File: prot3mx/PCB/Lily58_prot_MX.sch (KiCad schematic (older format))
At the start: 115 parts, among them J1 LED, J2 4PIN, J3 OLED, P1 i2c_pin, P2 i2c_pin, SW1 SW_PUSH, SW10 SW_PUSH, SW11 SW_PUSH, SW12 SW_PUSH, SW13 SW_PUSH, SW14 SW_PUSH, SW15 SW_PUSH, SW16 SW_PUSH, SW17 SW_PUSH, SW18 SW_PUSH, SW19 SW_PUSH, SW2 SW_PUSH, SW20 SW_PUSH, SW21 SW_PUSH, SW22 SW_PUSH, SW23 SW_PUSH, SW24 SW_PUSH, SW25 SW_PUSH, SW26 SW_PUSH, SW27 SW_PUSH, SW28 SW_PUSH, SW29 SW_PUSH, SW3 SW_PUSH, SW30 ROT_ENC_SW, SW31 ROT_ENC_SW, SW32 ROT_ENC_SW, SW4 SW_PUSH, SW5 SW_PUSH, SW6 SW_PUSH, SW7 SW_PUSH, SW8 SW_PUSH, SW9 SW_PUSH, U1 ProMicro

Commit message: repositioned diodes, using original LED footprints
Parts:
- L1, L10, L11, L12, L13, L14, L15, L16, L17, L18, L19, L2, L20, L21, L22, L23, L24, L25, L26, L27, L28, L29, L3, L4, L5, L6, L7, L8, L9: footprint Lily58_prot_MX-footprint:SK6812MINI_rev_w_co -> Lily58_prot_MX-footprint:SK6812MINI_rev
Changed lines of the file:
@@
 F 0 "L1" H 2650 3900 50  0000 L CNN
 F 1 "SK6812MINI" H 2400 3300 50  0000 L CNN
-F 2 "Lily58_prot_MX-footprint:SK6812MINI_rev_w_co" H 2650 3350 50  0001 L TNN
+F 2 "Lily58_prot_MX-footprint:SK6812MINI_rev" H 2650 3350 50  0001 L TNN
 F 3 "" H 2700 3275 50  0001 L TNN
 	1    2600 3650
@@
 F 0 "L2" H 3250 3900 50  0000 L CNN
 F 1 "SK6812MINI" H 3000 3300 50  0000 L CNN
-F 2 "Lily58_prot_MX-footprint:SK6812MINI_rev_w_co" H 3250 3350 50  0001 L TNN
+F 2 "Lily58_prot_MX-footprint:SK6812MINI_rev" H 3250 3350 50  0001 L TNN
 F 3 "" H 3300 3275 50  0001 L TNN
 	1    3200 3650
@@
 F 0 "L3" H 3850 3900 50  0000 L CNN
 F 1 "SK6812MINI" H 3600 3300 50  0000 L CNN
-F 2 "Lily58_prot_MX-footprint:SK6812MINI_rev_w_co" H 3850 3350 50  0001 L TNN
+F 2 "Lily58_prot_MX-footprint:SK6812MINI_rev" H 3850 3350 50  0001 L TNN
 F 3 "" H 3900 3275 50  0001 L TNN
 	1    3800 3650
@@
 F 0 "L4" H 4450 3900 50  0000 L CNN
 F 1 "SK6812MINI" H 4200 3300 50  0000 L CNN
-F 2 "Lily58_prot_MX-footprint:SK6812MINI_rev_w_co" H 4450 3350 50  0001 L TNN
+F 2 "Lily58_prot_MX-footprint:SK6812MINI_rev" H 4450 3350 50  0001 L TNN
 F 3 "" H 4500 3275 50  0001 L TNN
 	1    4400 3650
@@
 F 0 "L5" H 5050 3900 50  0000 L CNN
 F 1 "SK6812MINI" H 4800 3300 50  0000 L CNN
-F 2 "Lily58_prot_MX-footprint:SK6812MINI_rev_w_co" H 5050 3350 50  0001 L TNN
+F 2 "Lily58_prot_MX-footprint:SK6812MINI_rev" H 5050 3350 50  0001 L TNN
 F 3 "" H 5100 3275 50  0001 L TNN
 	1    5000 3650
@@
 F 0 "L6" H 5650 3900 50  0000 L CNN
 F 1 "SK6812MINI" H 5400 3300 50  0000 L CNN
-F 2 "Lily58_prot_MX-footprint:SK6812MINI_rev_w_co" H 5650 3350 50  0001 L TNN
+F 2 "Lily58_prot_MX-footprint:SK6812MINI_rev" H 5650 3350 50  0001 L TNN
 F 3 "" H 5700 3275 50  0001 L TNN
 	1    5600 3650
@@
 F 0 "L7" H 2650 4750 50  0000 L CNN
 F 1 "SK6812MINI" H 2400 4150 50  0000 L CNN
-F 2 "Lily58_prot_MX-footprint:SK6812MINI_rev_w_co" H 2650 4200 50  0001 L TNN
+F 2 "Lily58_prot_MX-footprint:SK6812MINI_rev" H 2650 4200 50  0001 L TNN
 F 3 "" H 2700 4125 50  0001 L TNN
 	1    2600 4500
@@
 F 0 "L8" H 3250 4750 50  0000 L CNN
 F 1 "SK6812MINI" H 3000 4150 50  0000 L CNN
-F 2 "Lily58_prot_MX-footprint:SK6812MINI_rev_w_co" H 3250 4200 50  0001 L TNN
+F 2 "Lily58_prot_MX-footprint:SK6812MINI_rev" H 3250 4200 50  0001 L TNN
 F 3 "" H 3300 4125 50  0001 L TNN
 	1    3200 4500
@@
 F 0 "L9" H 3850 4750 50  0000 L CNN
 F 1 "SK6812MINI" H 3600 4150 50  0000 L CNN
-F 2 "Lily58_prot_MX-footprint:SK6812MINI_rev_w_co" H 3850 4200 50  0001 L TNN
+F 2 "Lily58_prot_MX-footprint:SK6812MINI_rev" H 3850 4200 50  0001 L TNN
 F 3 "" H 3900 4125 50  0001 L TNN
 	1    3800 4500
@@
 F 0 "L10" H 4450 4750 50  0000 L CNN
 F 1 "SK6812MINI" H 4200 4150 50  0000 L CNN
-F 2 "Lily58_prot_MX-footprint:SK6812MINI_rev_w_co" H 4450 4200 50  0001 L TNN
+F 2 "Lily58_prot_MX-footprint:SK6812MINI_rev" H 4450 4200 50  0001 L TNN
 F 3 "" H 4500 4125 50  0001 L TNN
 	1    4400 4500
@@
 F 0 "L11" H 5050 4750 50  0000 L CNN
 F 1 "SK6812MINI" H 4800 4150 50  0000 L CNN
-F 2 "Lily58_prot_MX-footprint:SK6812MINI_rev_w_co" H 5050 4200 50  0001 L TNN
+F 2 "Lily58_prot_MX-footprint:SK6812MINI_rev" H 5050 4200 50  0001 L TNN
 F 3 "" H 5100 4125 50  0001 L TNN
 	1    5000 4500
@@
 F 0 "L12" H 5650 4750 50  0000 L CNN
 F 1 "SK6812MINI" H 5400 4150 50  0000 L CNN
-F 2 "Lily58_prot_MX-footprint:SK6812MINI_rev_w_co" H 5650 4200 50  0001 L TNN
+F 2 "Lily58_prot_MX-footprint:SK6812MINI_rev" H 5650 4200 50  0001 L TNN
 F 3 "" H 5700 4125 50  0001 L TNN
 	1    5600 4500
@@
 F 0 "L13" H 2650 5600 50  0000 L CNN
 F 1 "SK6812MINI" H 2400 5000 50  0000 L CNN
-F 2 "Lily58_prot_MX-footprint:SK6812MINI_rev_w_co" H 2650 5050 50  0001 L TNN
+F 2 "Lily58_prot_MX-footprint:SK6812MINI_rev" H 2650 5050 50  0001 L TNN
 F 3 "" H 2700 4975 50  0001 L TNN
 	1    2600 5350
@@
 F 0 "L14" H 3250 5600 50  0000 L CNN
 F 1 "SK6812MINI" H 3000 5000 50  0000 L CNN
-F 2 "Lily58_prot_MX-footprint:SK6812MINI_rev_w_co" H 3250 5050 50  0001 L TNN
+F 2 "Lily58_prot_MX-footprint:SK6812MINI_rev" H 3250 5050 50  0001 L TNN
 F 3 "" H 3300 4975 50  0001 L TNN
 	1    3200 5350
@@
 F 0 "L15" H 3850 5600 50  0000 L CNN
 F 1 "SK6812MINI" H 3600 5000 50  0000 L CNN
-F 2 "Lily58_prot_MX-footprint:SK6812MINI_rev_w_co" H 3850 5050 50  0001 L TNN
+F 2 "Lily58_prot_MX-footprint:SK6812MINI_rev" H 3850 5050 50  0001 L TNN
 F 3 "" H 3900 4975 50  0001 L TNN
 	1    3800 5350
@@
 F 0 "L16" H 4450 5600 50  0000 L CNN
 F 1 "SK6812MINI" H 4200 5000 50  0000 L CNN
-F 2 "Lily58_prot_MX-footprint:SK6812MINI_rev_w_co" H 4450 5050 50  0001 L TNN
+F 2 "Lily58_prot_MX-footprint:SK6812MINI_rev" H 4450 5050 50  0001 L TNN
 F 3 "" H 4500 4975 50  0001 L TNN
 	1    4400 5350
@@
 F 0 "L17" H 5050 5600 50  0000 L CNN
 F 1 "SK6812MINI" H 4800 5000 50  0000 L CNN
-F 2 "Lily58_prot_MX-footprint:SK6812MINI_rev_w_co" H 5050 5050 50  0001 L TNN
+F 2 "Lily58_prot_MX-footprint:SK6812MINI_rev" H 5050 5050 50  0001 L TNN
 F 3 "" H 5100 4975 50  0001 L TNN
 	1    5000 5350
@@
 F 0 "L18" H 5650 5600 50  0000 L CNN
 F 1 "SK6812MINI" H 5400 5000 50  0000 L CNN
-F 2 "Lily58_prot_MX-footprint:SK6812MINI_rev_w_co" H 5650 5050 50  0001 L TNN
+F 2 "Lily58_prot_MX-footprint:SK6812MINI_rev" H 5650 5050 50  0001 L TNN
 F 3 "" H 5700 4975 50  0001 L TNN
 	1    5600 5350
@@
 F 0 "L19" H 2650 6450 50  0000 L CNN
 F 1 "SK6812MINI" H 2400 5850 50  0000 L CNN
-F 2 "Lily58_prot_MX-footprint:SK6812MINI_rev_w_co" H 2650 5900 50  0001 L TNN
+F 2 "Lily58_prot_MX-footprint:SK6812MINI_rev" H 2650 5900 50  0001 L TNN
 F 3 "" H 2700 5825 50  0001 L TNN
 	1    2600 6200
@@
 F 0 "L20" H 3250 6450 50  0000 L CNN
 F 1 "SK6812MINI" H 3000 5850 50  0000 L CNN
-F 2 "Lily58_prot_MX-footprint:SK6812MINI_rev_w_co" H 3250 5900 50  0001 L TNN
+F 2 "Lily58_prot_MX-footprint:SK6812MINI_rev" H 3250 5900 50  0001 L TNN
 F 3 "" H 3300 5825 50  0001 L TNN
 	1    3200 6200
@@
 F 0 "L21" H 3850 6450 50  0000 L CNN
 F 1 "SK6812MINI" H 3600 5850 50  0000 L CNN
-F 2 "Lily58_prot_MX-footprint:SK6812MINI_rev_w_co" H 3850 5900 50  0001 L TNN
+F 2 "Lily58_prot_MX-footprint:SK6812MINI_rev" H 3850 5900 50  0001 L TNN
 F 3 "" H 3900 5825 50  0001 L TNN
 	1    3800 6200
@@
 F 0 "L22" H 4450 6450 50  0000 L CNN
 F 1 "SK6812MINI" H 4200 5850 50  0000 L CNN
-F 2 "Lily58_prot_MX-footprint:SK6812MINI_rev_w_co" H 4450 5900 50  0001 L TNN
+F 2 "Lily58_prot_MX-footprint:SK6812MINI_rev" H 4450 5900 50  0001 L TNN
 F 3 "" H 4500 5825 50  0001 L TNN
 	1    4400 6200
@@
 F 0 "L23" H 5050 6450 50  0000 L CNN
 F 1 "SK6812MINI" H 4800 5850 50  0000 L CNN
-F 2 "Lily58_prot_MX-footprint:SK6812MINI_rev_w_co" H 5050 5900 50  0001 L TNN
+F 2 "Lily58_prot_MX-footprint:SK6812MINI_rev" H 5050 5900 50  0001 L TNN
 F 3 "" H 5100 5825 50  0001 L TNN
 	1    5000 6200
@@
 F 0 "L24" H 5650 6450 50  0000 L CNN
 F 1 "SK6812MINI" H 5400 5850 50  0000 L CNN
-F 2 "Lily58_prot_MX-footprint:SK6812MINI_rev_w_co" H 5650 5900 50  0001 L TNN
+F 2 "Lily58_prot_MX-footprint:SK6812MINI_rev" H 5650 5900 50  0001 L TNN
 F 3 "" H 5700 5825 50  0001 L TNN
 	1    5600 6200
@@
 F 0 "L25" H 2650 7300 50  0000 L CNN
 F 1 "SK6812MINI" H 2400 6700 50  0000 L CNN
-F 2 "Lily58_prot_MX-footprint:SK6812MINI_rev_w_co" H 2650 6750 50  0001 L TNN
+F 2 "Lily58_prot_MX-footprint:SK6812MINI_rev" H 2650 6750 50  0001 L TNN
 F 3 "" H 2700 6675 50  0001 L TNN
 	1    2600 7050
@@
 F 0 "L26" H 3250 7300 50  0000 L CNN
 F 1 "SK6812MINI" H 3000 6700 50  0000 L CNN
-F 2 "Lily58_prot_MX-footprint:SK6812MINI_rev_w_co" H 3250 6750 50  0001 L TNN
+F 2 "Lily58_prot_MX-footprint:SK6812MINI_rev" H 3250 6750 50  0001 L TNN
 F 3 "" H 3300 6675 50  0001 L TNN
 	1    3200 7050
@@
 F 0 "L27" H 3850 7300 50  0000 L CNN
 F 1 "SK6812MINI" H 3600 6700 50  0000 L CNN
-F 2 "Lily58_prot_MX-footprint:SK6812MINI_rev_w_co" H 3850 6750 50  0001 L TNN
+F 2 "Lily58_prot_MX-footprint:SK6812MINI_rev" H 3850 6750 50  0001 L TNN
 F 3 "" H 3900 6675 50  0001 L TNN
 	1    3800 7050
@@
 F 0 "L28" H 4450 7300 50  0000 L CNN
 F 1 "SK6812MINI" H 4200 6700 50  0000 L CNN
-F 2 "Lily58_prot_MX-footprint:SK6812MINI_rev_w_co" H 4450 6750 50  0001 L TNN
+F 2 "Lily58_prot_MX-footprint:SK6812MINI_rev" H 4450 6750 50  0001 L TNN
 F 3 "" H 4500 6675 50  0001 L TNN
 	1    4400 7050
@@
 F 0 "L29" H 5050 7300 50  0000 L CNN
 F 1 "SK6812MINI" H 4800 6700 50  0000 L CNN
-F 2 "Lily58_prot_MX-footprint:SK6812MINI_rev_w_co" H 5050 6750 50  0001 L TNN
+F 2 "Lily58_prot_MX-footprint:SK6812MINI_rev" H 5050 6750 50  0001 L TNN
 F 3 "" H 5100 6675 50  0001 L TNN
 	1    5000 7050

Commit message: replaced hotswap footprint with TH footprint where encoder footprint overlaps
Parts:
- SW25, SW29, SW6: footprint Lily58_prot_MX-footprint:MX_Hotswap -> Lily58_prot_MX-footprint:MX_FLIP_HOLES
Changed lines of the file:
@@
 F 0 "SW25" H 6650 3700 50  0000 C CNN
 F 1 "SW_PUSH" H 6650 3450 50  0000 C CNN
-F 2 "Lily58_prot_MX-footprint:MX_Hotswap" H 6650 3550 50  0001 C CNN
+F 2 "Lily58_prot_MX-footprint:MX_FLIP_HOLES" H 6650 3550 50  0001 C CNN
 F 3 "" H 6650 3550 50  0000 C CNN
 	1    6650 3550
@@
 F 0 "SW6" H 10650 1400 50  0000 C CNN
 F 1 "SW_PUSH" H 10650 1200 50  0000 C CNN
-F 2 "Lily58_prot_MX-footprint:MX_Hotswap" H 10650 1250 50  0001 C CNN
+F 2 "Lily58_prot_MX-footprint:MX_FLIP_HOLES" H 10650 1250 50  0001 C CNN
 F 3 "" H 10650 1250 50  0000 C CNN
 	1    10650 1250
@@
 F 0 "SW29" H 9850 3700 50  0000 C CNN
 F 1 "SW_PUSH" H 9850 3450 50  0000 C CNN
-F 2 "Lily58_prot_MX-footprint:MX_Hotswap" H 9850 3550 50  0001 C CNN
+F 2 "Lily58_prot_MX-footprint:MX_FLIP_HOLES" H 9850 3550 50  0001 C CNN
 F 3 "" H 9850 3550 50  0000 C CNN
 	1    9850 3550

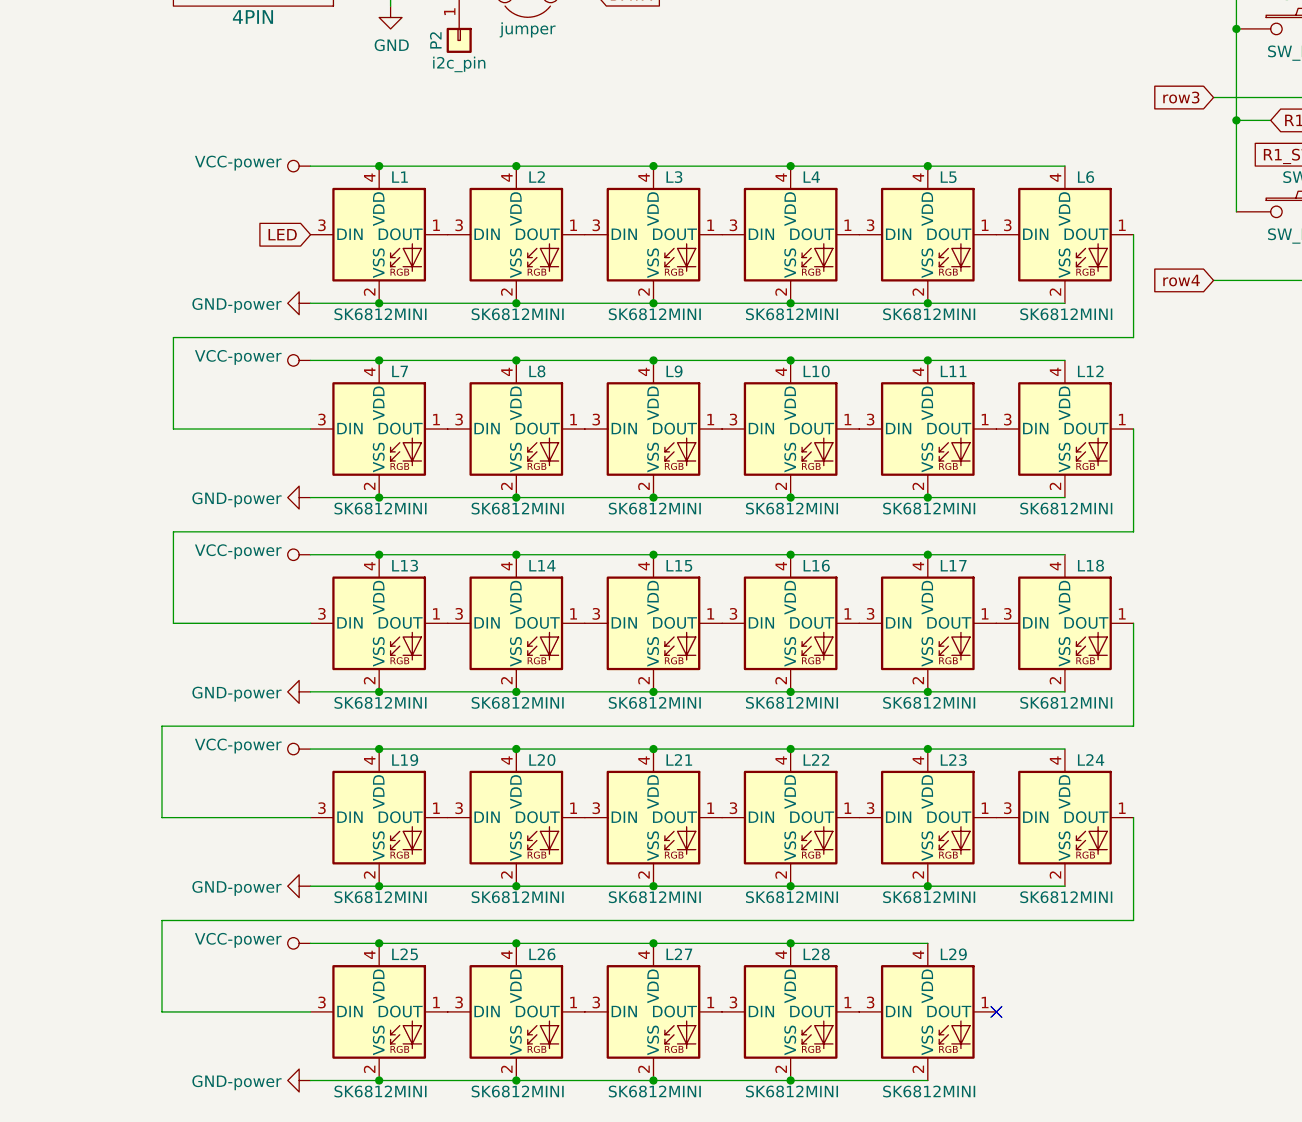
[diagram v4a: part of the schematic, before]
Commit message: removed per-key-LEG in favour of underglow only
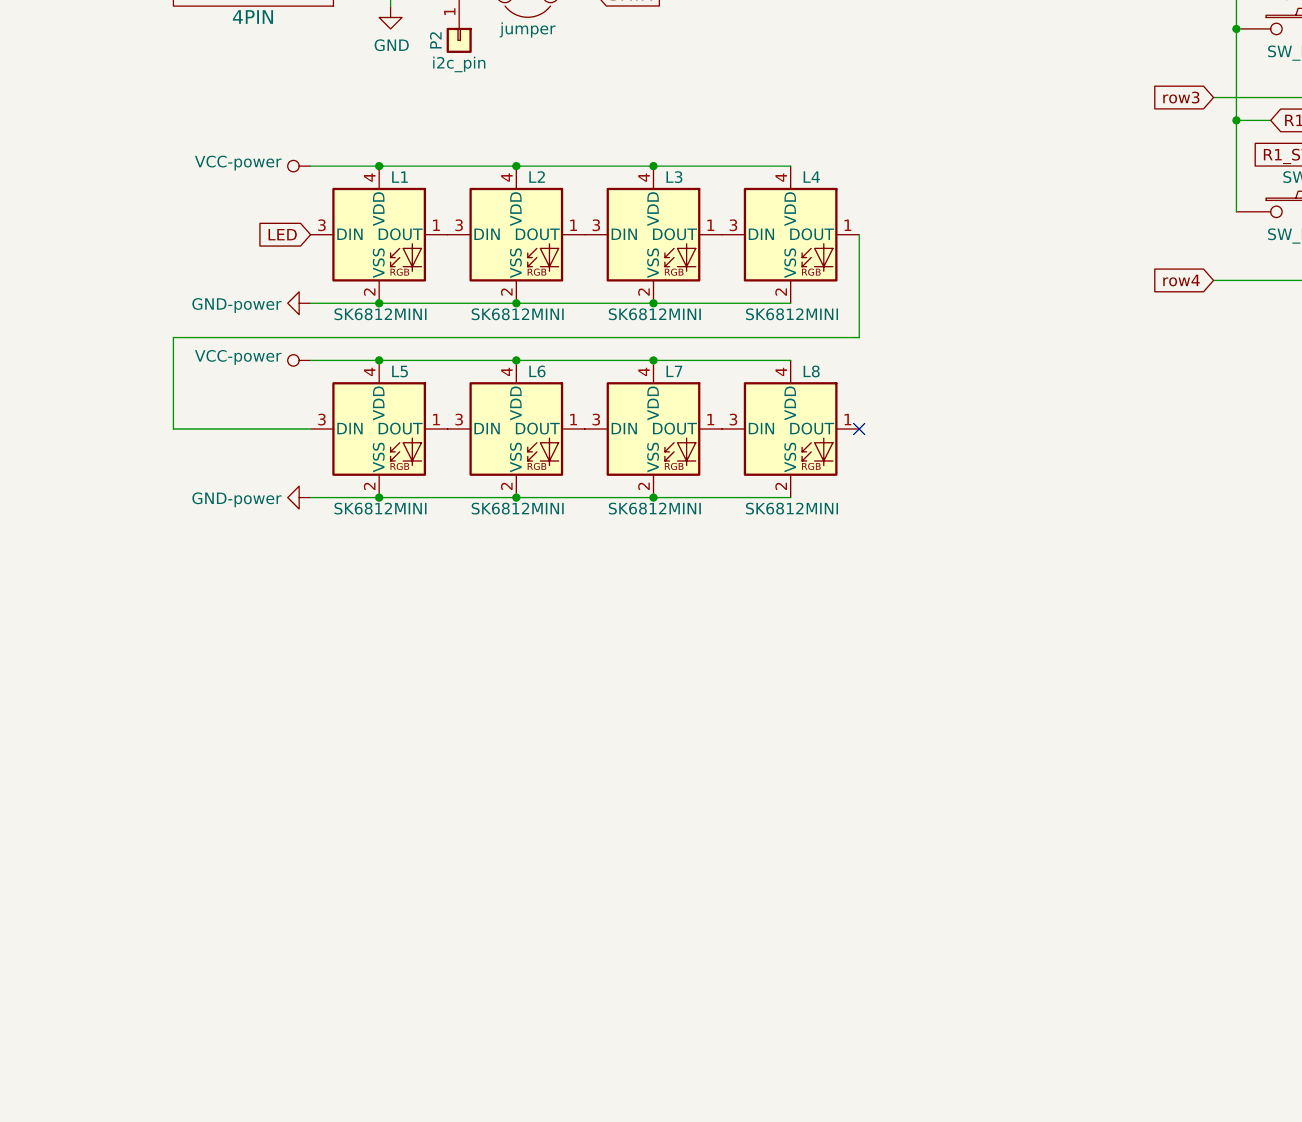
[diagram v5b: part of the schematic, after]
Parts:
- removed L11, L12, L13, L14, L15, L16, L17, L18, L19, L20, L21, L22, L23, L24, L25, L26, L27, L28, L29, L5, L6: SK6812MINI, Lily58_prot_MX-footprint:SK6812MINI_rev, symbol Lily58_prot_MX-rescue:LED_SK6812MINI
- L1, L2, L3, L4: footprint Lily58_prot_MX-footprint:SK6812MINI_rev -> Lily58_prot_MX-footprint:SK6812MINI_underglow_rev
- L5: renamed from L7; footprint Lily58_prot_MX-footprint:SK6812MINI_rev -> Lily58_prot_MX-footprint:SK6812MINI_underglow_rev
- L6: renamed from L8; footprint Lily58_prot_MX-footprint:SK6812MINI_rev -> Lily58_prot_MX-footprint:SK6812MINI_underglow_rev
- L7: renamed from L9; footprint Lily58_prot_MX-footprint:SK6812MINI_rev -> Lily58_prot_MX-footprint:SK6812MINI_underglow_rev
- L8: renamed from L10; footprint Lily58_prot_MX-footprint:SK6812MINI_rev -> Lily58_prot_MX-footprint:SK6812MINI_underglow_rev
- SW25, SW29, SW6: footprint Lily58_prot_MX-footprint:MX_FLIP_HOLES -> Lily58_prot_MX-footprint:MX_Hotswap
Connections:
- net at L4.1 (DOUT): now also L5.3 (DIN)
